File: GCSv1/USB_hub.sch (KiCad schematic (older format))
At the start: 8 parts

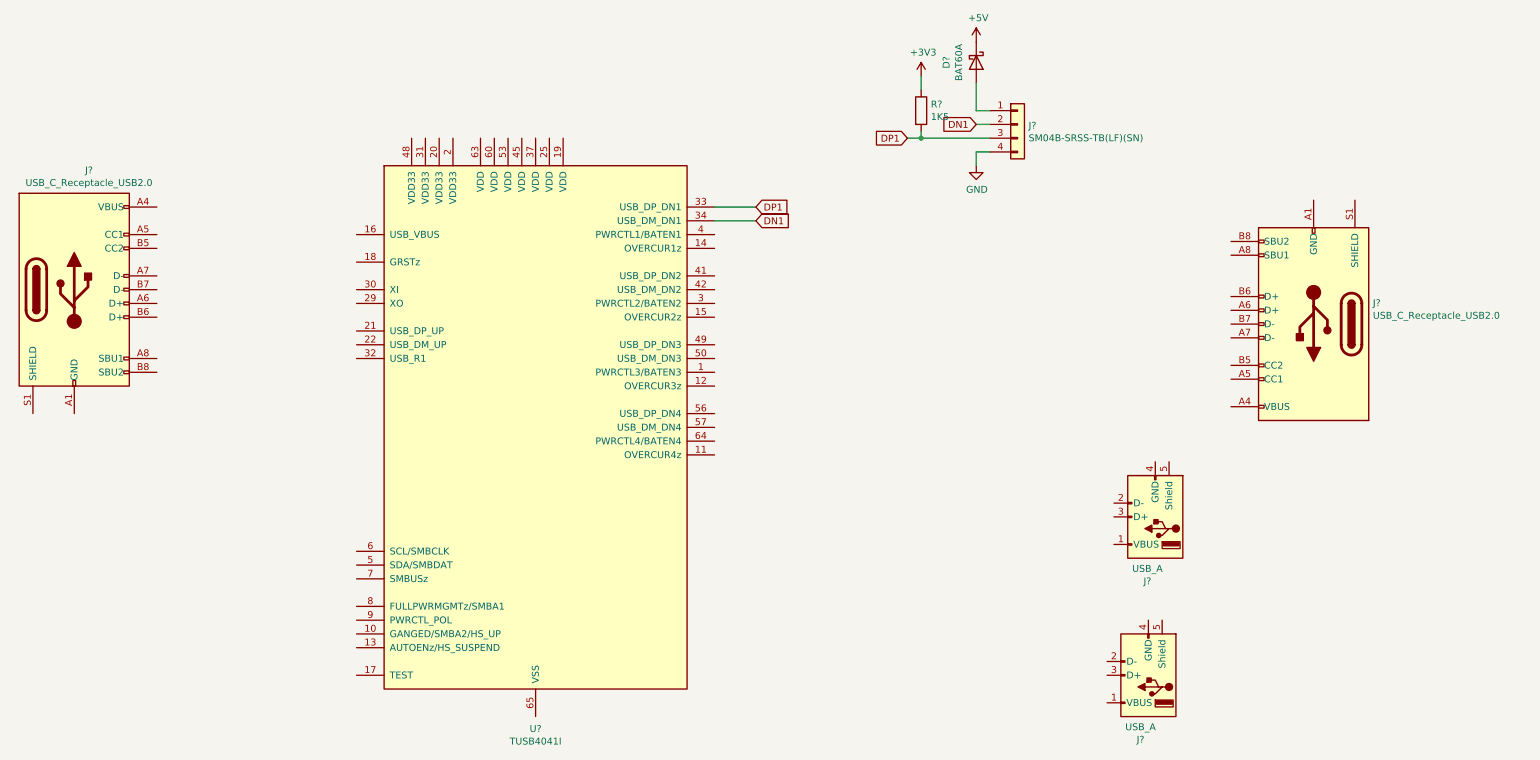
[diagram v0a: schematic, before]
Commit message: going to use two USB C Daughterboards
after doing some research into connecting a USB C connector to the USB 2.0 hub, I looked at the KiCad project for the Daughterboard and saw that an overcurrent protection circuit, IC, and ferrite bead were used to connect to the JST connector. I've decided just use two of the Daughterboards, one for upstream and the other downstream
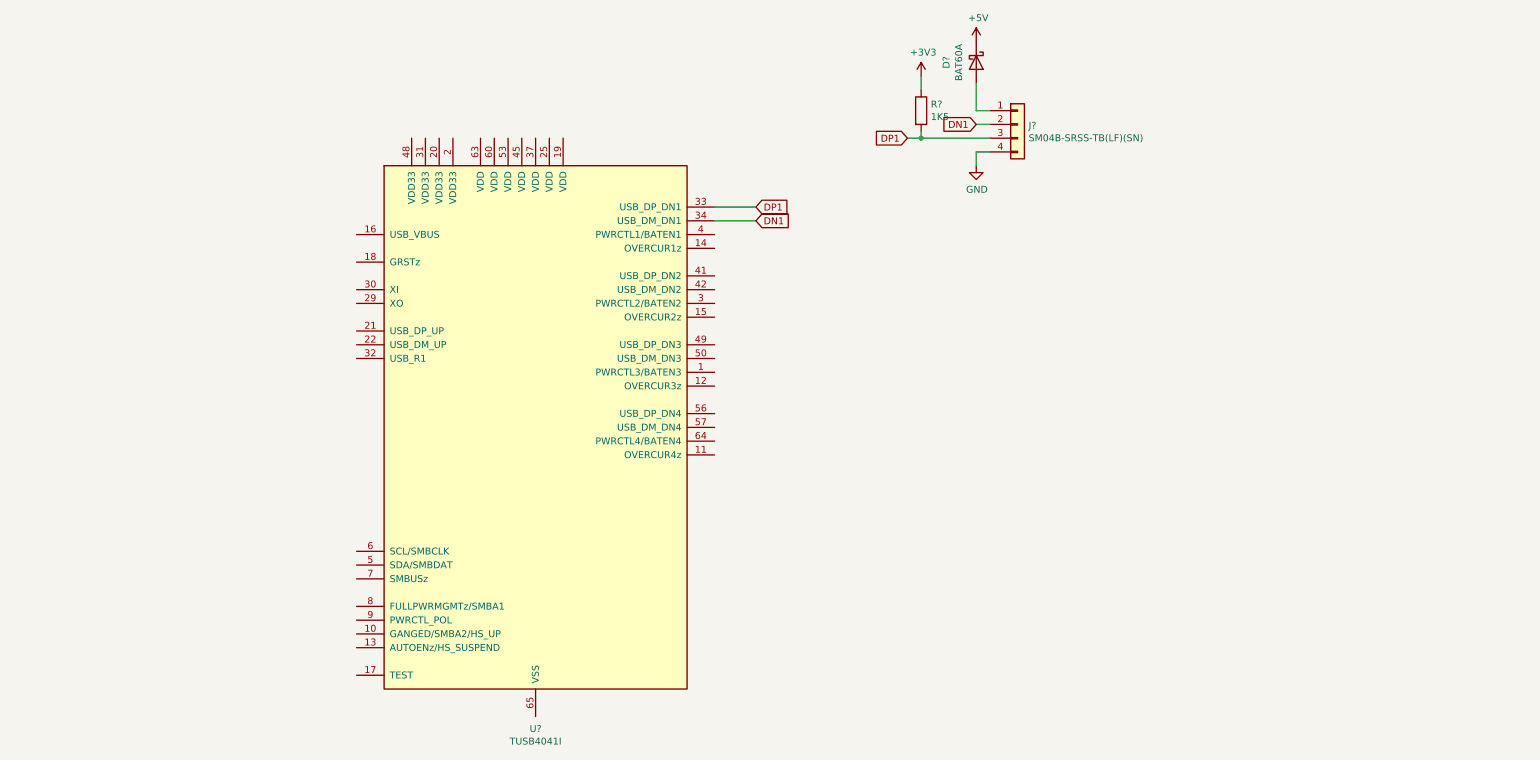
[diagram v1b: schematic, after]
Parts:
- removed J? (x2): USB_C_Receptacle_USB2.0, symbol Connector:USB_C_Receptacle_USB2.0
- removed J? (x2): USB_A, symbol Connector:USB_A
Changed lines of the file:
@@
 Text GLabel 6050 2150 2    50   Input ~ 0
 DN1
-$Comp
-L Connector:USB_C_Receptacle_USB2.0 J?
-U 1 1 6120F989
-P 1100 2650
-F 0 "J?" H 1207 3517 50  0000 C CNN
-F 1 "USB_C_Receptacle_USB2.0" H 1207 3426 50  0000 C CNN
-F 2 "" H 1250 2650 50  0001 C CNN
-F 3 "https://www.usb.org/sites/default/files/documents/usb_type-c.zip" H 1250 2650 50  0001 C CNN
-	1    1100 2650
-	1    0    0    -1
-$EndComp
-$Comp
-L Connector:USB_C_Receptacle_USB2.0 J?
-U 1 1 61212A11
-P 10100 2900
-F 0 "J?" H 9670 2747 50  0000 R CNN
-F 1 "USB_C_Receptacle_USB2.0" H 9670 2838 50  0000 R CNN
-F 2 "" H 10250 2900 50  0001 C CNN
-F 3 "https://www.usb.org/sites/default/files/documents/usb_type-c.zip" H 10250 2900 50  0001 C CNN
-	1    10100 2900
-	-1   0    0    1
-$EndComp
-$Comp
-L Connector:USB_A J?
-U 1 1 612169A9
-P 8950 4300
-F 0 "J?" H 9007 4767 50  0000 C CNN
-F 1 "USB_A" H 9007 4676 50  0000 C CNN
-F 2 "" H 9100 4250 50  0001 C CNN
-F 3 " ~" H 9100 4250 50  0001 C CNN
-	1    8950 4300
-	-1   0    0    1
-$EndComp
-$Comp
-L Connector:USB_A J?
-U 1 1 6121D6E4
-P 8900 5450
-F 0 "J?" H 8957 5917 50  0000 C CNN
-F 1 "USB_A" H 8957 5826 50  0000 C CNN
-F 2 "" H 9050 5400 50  0001 C CNN
-F 3 " ~" H 9050 5400 50  0001 C CNN
-	1    8900 5450
-	-1   0    0    1
-$EndComp
 $EndSCHEMATC
